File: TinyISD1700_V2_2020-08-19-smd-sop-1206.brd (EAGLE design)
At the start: 45.5 x 45.1 mm, 18 parts, among them IC3 LM317MDT, U1 ATTINY4313-SU

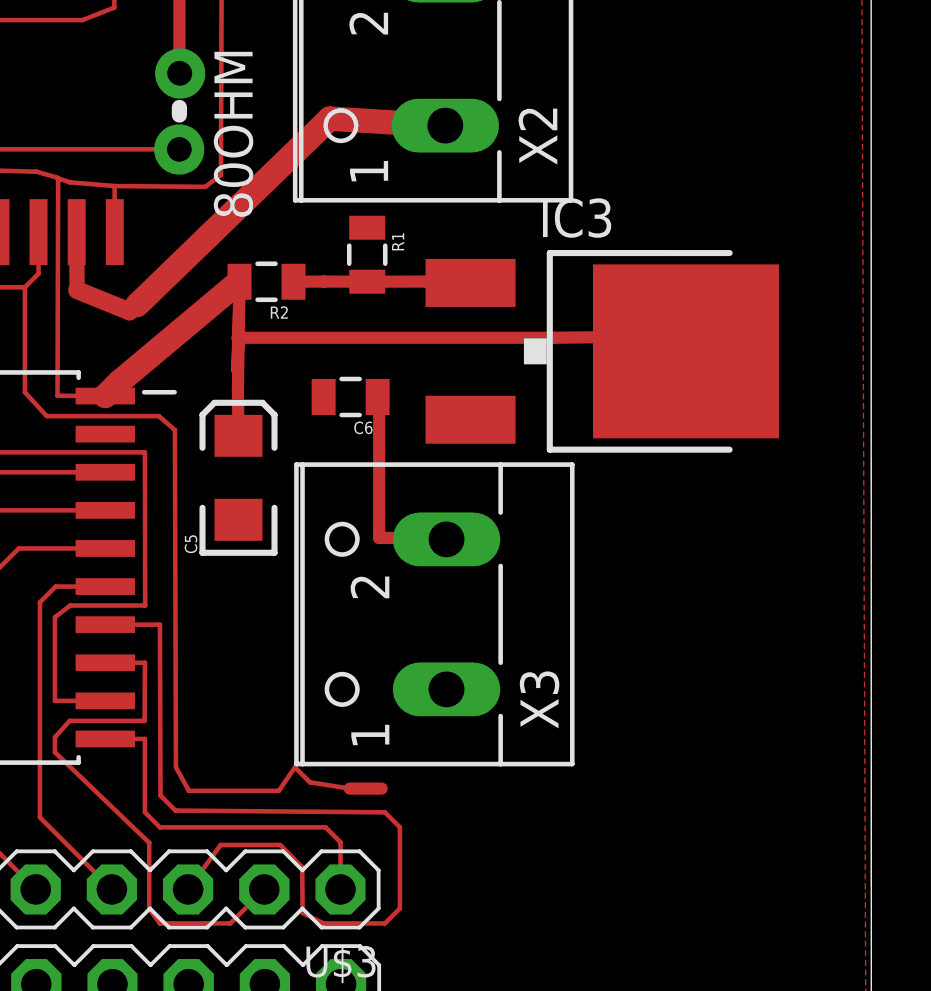
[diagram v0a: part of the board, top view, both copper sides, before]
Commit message: Resistors changed to 1205 factor
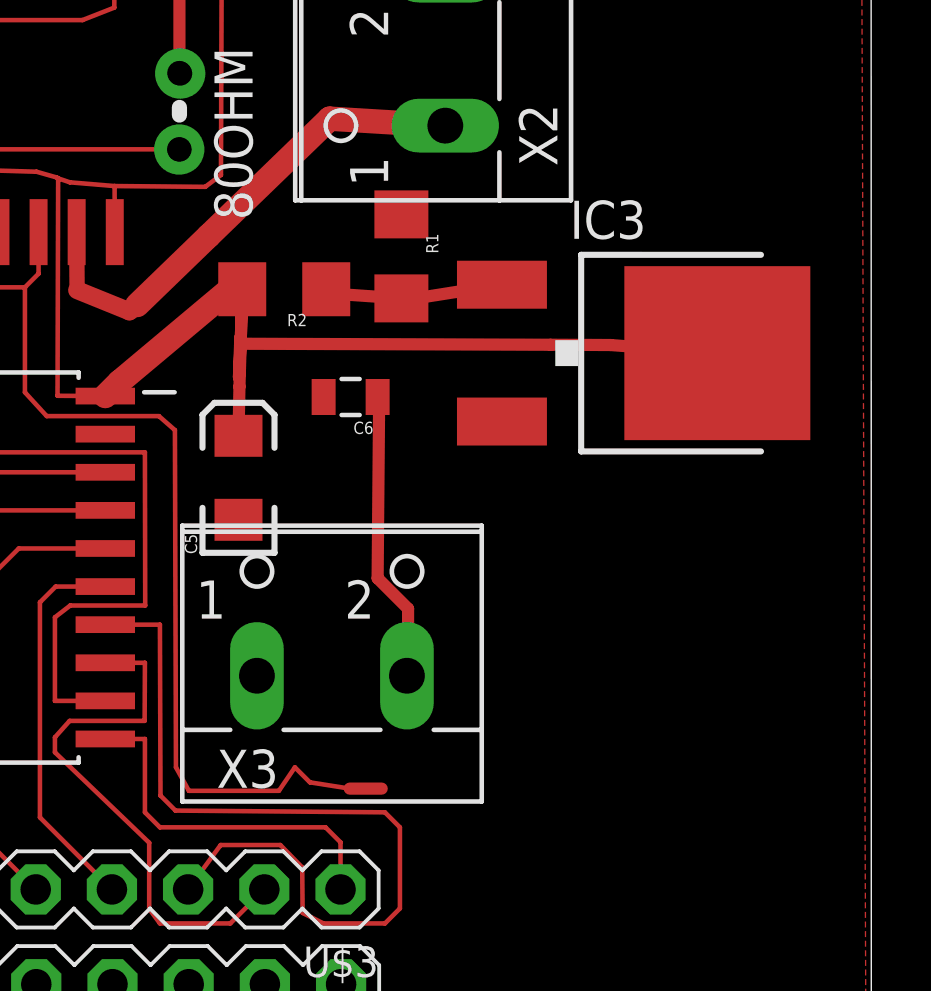
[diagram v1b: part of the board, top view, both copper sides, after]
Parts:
- R1, R2: device SparkFun2:0805 -> SparkFun:1206
- moved X3 2.67 mm to (25.5, 12.7), turned to 0 degrees
- moved R1 1.14 mm to (27.8, 25.5)
- moved IC3 1.05 mm to (36.0, 22.2)
- moved R2 0.64 mm to (23.9, 24.4)
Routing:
- net N$28: track 7.04 -> 9.80 mm
- net VCC: track 88.8 -> 89.8 mm
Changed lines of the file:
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@@
 <layer number="17" name="Pads" color="2" fill="1" visible="yes" active="yes"/>
 <layer number="18" name="Vias" color="2" fill="1" visible="yes" active="yes"/>
-<layer number="19" name="Unrouted" color="6" fill="1" visible="no" active="yes"/>
+<layer number="19" name="Unrouted" color="6" fill="1" visible="yes" active="yes"/>
 <layer number="20" name="Dimension" color="15" fill="1" visible="no" active="yes"/>
 <layer number="21" name="tPlace" color="7" fill="1" visible="no" active="yes"/>
 <layer number="22" name="bPlace" color="7" fill="1" visible="no" active="yes"/>
-<layer number="23" name="tOrigins" color="15" fill="1" visible="no" active="yes"/>
-<layer number="24" name="bOrigins" color="15" fill="1" visible="no" active="yes"/>
+<layer number="23" name="tOrigins" color="15" fill="1" visible="yes" active="yes"/>
+<layer number="24" name="bOrigins" color="15" fill="1" visible="yes" active="yes"/>
 <layer number="25" name="tNames" color="7" fill="1" visible="no" active="yes"/>
 <layer number="26" name="bNames" color="7" fill="1" visible="no" active="yes"/>
@@
 <attribute name="VALUE" x="35.6541875" y="27.271328125" size="1.27" layer="27" ratio="10" rot="R90"/>
 </element>
-<element name="X3" library="con-wago-500" package="W237-102" value="" x="28.07615" y="13.518975" smashed="yes" rot="R90">
-<attribute name="MF" value="" x="28.07615" y="13.518975" size="1.778" layer="27" rot="R90" display="off"/>
-<attribute name="MPN" value="" x="28.07615" y="13.518975" size="1.778" layer="27" rot="R90" display="off"/>
-<attribute name="NAME" x="33.07995" y="9.672775" size="1.27" layer="25" ratio="10" rot="R90"/>
-<attribute name="OC_FARNELL" value="unknown" x="28.07615" y="13.518975" size="1.778" layer="27" rot="R90" display="off"/>
-<attribute name="OC_NEWARK" value="70K9898" x="28.07615" y="13.518975" size="1.778" layer="27" rot="R90" display="off"/>
-<attribute name="VALUE" x="35.69615" y="8.478975" size="1.27" layer="27" ratio="10" rot="R90"/>
+<element name="X3" library="con-wago-500" package="W237-102" value="" x="25.525759375" y="12.74339375" smashed="yes">
+<attribute name="MF" value="" x="25.525759375" y="12.74339375" size="1.778" layer="27" display="off"/>
+<attribute name="MPN" value="" x="25.525759375" y="12.74339375" size="1.778" layer="27" display="off"/>
+<attribute name="NAME" x="21.679559375" y="7.73959375" size="1.27" layer="25" ratio="10"/>
+<attribute name="OC_FARNELL" value="unknown" x="25.525759375" y="12.74339375" size="1.778" layer="27" display="off"/>
+<attribute name="OC_NEWARK" value="70K9898" x="25.525759375" y="12.74339375" size="1.778" layer="27" display="off"/>
+<attribute name="VALUE" x="20.485759375" y="5.12339375" size="1.27" layer="27" ratio="10"/>
 </element>
 <element name="C6" library="SparkFun2" package="0805" value="" x="26.1483375" y="20.76579375" smashed="yes" rot="R180">
@@
 <attribute name="VALUE" x="27.1643375" y="22.16279375" size="0.4064" layer="27" rot="R180"/>
 </element>
-<element name="R1" library="SparkFun2" package="0805" value="" x="26.7023125" y="25.50895" smashed="yes" rot="R270">
-<attribute name="NAME" x="27.5278125" y="26.27095" size="0.4064" layer="25" rot="R270"/>
-<attribute name="VALUE" x="25.3053125" y="26.52495" size="0.4064" layer="27" rot="R270"/>
-</element>
-<element name="R2" library="SparkFun2" package="0805" value="" x="23.34449375" y="24.606784375" smashed="yes" rot="R180">
-<attribute name="NAME" x="24.10649375" y="23.781284375" size="0.4064" layer="25" rot="R180"/>
-<attribute name="VALUE" x="24.36049375" y="26.003784375" size="0.4064" layer="27" rot="R180"/>
+<element name="R1" library="SparkFun" package="1206" value="" x="27.840146875" y="25.45298125" smashed="yes" rot="R270">
+<attribute name="NAME" x="28.665646875" y="26.21498125" size="0.4064" layer="25" rot="R270"/>
+<attribute name="VALUE" x="26.443146875" y="26.46898125" size="0.4064" layer="27" rot="R270"/>
+</element>
+<element name="R2" library="SparkFun" package="1206" value="" x="23.93505625" y="24.358078125" smashed="yes" rot="R180">
+<attribute name="NAME" x="24.69705625" y="23.532578125" size="0.4064" layer="25" rot="R180"/>
+<attribute name="VALUE" x="24.95105625" y="25.755078125" size="0.4064" layer="27" rot="R180"/>
 </element>
 <element name="C5" library="SparkFun2" package="EIA3216" value="" x="22.410459375" y="18.071790625" smashed="yes" rot="R90">
@@
 <attribute name="VALUE" x="21.078459375" y="18.479790625" size="0.4064" layer="27" rot="R90"/>
 </element>
-<element name="IC3" library="v-reg" package="DPACK" value="LM317MDT" x="34.94599375" y="22.287078125" rot="R270"/>
+<element name="IC3" library="v-reg" package="DPACK" value="LM317MDT" x="35.991984375" y="22.228065625" rot="R270"/>
 <element name="U$1" library="arduino" package="8PIN_HEADER" value="8PIN_HEADER" x="8.050165625" y="1.192378125">
 <attribute name="MPN" value="YSDKS128E10" x="8.050165625" y="1.192378125" size="1.778" layer="27" display="off"/>
@@
 <contactref element="R2" pad="2"/>
 <contactref element="C5" pad="A"/>
-<wire x1="22.44449375" y1="24.606784375" x2="22.390965625" y2="20.996465625" width="0.4064" layer="1"/>
-<wire x1="22.410459375" y1="19.471790625" x2="22.390965625" y2="20.996465625" width="0.4064" layer="1"/>
-<wire x1="22.44449375" y1="24.606784375" x2="22.29029375" y2="24.49384375" width="0.4064" layer="1"/>
-<wire x1="22.44449375" y1="24.606784375" x2="22.400828125" y2="22.8057875" width="0.4064" layer="1"/>
-<wire x1="22.400828125" y1="22.8057875" x2="22.37325" y2="21.668340625" width="0.4064" layer="1"/>
-<wire x1="22.37325" y1="21.668340625" x2="22.4187875" y2="22.989696875" width="0.4064" layer="1"/>
+<wire x1="22.53505625" y1="24.358078125" x2="22.442771875" y2="21.113009375" width="0.4064" layer="1"/>
+<wire x1="22.410459375" y1="19.471790625" x2="22.442771875" y2="21.113009375" width="0.4064" layer="1"/>
+<wire x1="22.53505625" y1="24.358078125" x2="22.29029375" y2="24.49384375" width="0.4064" layer="1"/>
+<wire x1="22.53505625" y1="24.358078125" x2="22.491484375" y2="22.7928375" width="0.4064" layer="1"/>
+<wire x1="22.491484375" y1="22.7928375" x2="22.425053125" y2="21.422303125" width="0.4064" layer="1"/>
+<wire x1="22.425053125" y1="21.422303125" x2="22.470590625" y2="22.743659375" width="0.4064" layer="1"/>
 <contactref element="IC3" pad="4"/>
-<wire x1="37.32599375" y1="22.287078125" x2="34.856428125" y2="22.7624625" width="0.4064" layer="1"/>
-<wire x1="34.856428125" y1="22.7624625" x2="32.916465625" y2="22.740228125" width="0.4064" layer="1"/>
-<wire x1="32.916465625" y1="22.740228125" x2="22.381428125" y2="22.740228125" width="0.4064" layer="1"/>
-<wire x1="22.381428125" y1="22.740228125" x2="22.400828125" y2="22.8057875" width="0.4064" layer="1"/>
+<wire x1="38.371984375" y1="22.228065625" x2="34.814984375" y2="22.4982875" width="0.4064" layer="1"/>
+<wire x1="34.814984375" y1="22.4982875" x2="32.81285625" y2="22.507140625" width="0.4064" layer="1"/>
+<wire x1="32.81285625" y1="22.507140625" x2="22.472084375" y2="22.540746875" width="0.4064" layer="1"/>
+<wire x1="22.472084375" y1="22.540746875" x2="22.491484375" y2="22.7928375" width="0.4064" layer="1"/>
 </signal>
 <signal name="Q">
@@
 <contactref element="R1" pad="2"/>
 <contactref element="R2" pad="1"/>
-<wire x1="24.24449375" y1="24.606784375" x2="25.2648625" y2="24.61429375" width="0.4064" layer="1"/>
-<wire x1="25.2648625" y1="24.61429375" x2="26.7023125" y2="24.60895" width="0.4064" layer="1"/>
-<wire x1="26.7023125" y1="24.60895" x2="28.741184375" y2="24.61429375" width="0.4064" layer="1"/>
+<wire x1="25.33505625" y1="24.358078125" x2="25.135353125" y2="24.238765625" width="0.4064" layer="1"/>
+<wire x1="25.135353125" y1="24.238765625" x2="27.840146875" y2="24.05298125" width="0.4064" layer="1"/>
+<wire x1="27.840146875" y1="24.05298125" x2="27.938225" y2="23.91503125" width="0.4064" layer="1"/>
 <contactref element="IC3" pad="1"/>
-<wire x1="30.14599375" y1="24.567078125" x2="28.741184375" y2="24.567078125" width="0.4064" layer="1"/>
-<wire x1="28.741184375" y1="24.567078125" x2="28.741184375" y2="24.61429375" width="0.4064" layer="1"/>
+<wire x1="31.191984375" y1="24.508065625" x2="28.041834375" y2="24.010259375" width="0.4064" layer="1"/>
+<wire x1="28.041834375" y1="24.010259375" x2="27.938225" y2="23.91503125" width="0.4064" layer="1"/>
 </signal>
 <signal name="N$28">
@@
 <contactref element="X3" pad="2"/>
 <wire x1="27.0483375" y1="20.76579375" x2="27.099721875" y2="20.76579375" width="0.4064" layer="1"/>
-<wire x1="27.099721875" y1="20.76579375" x2="27.099721875" y2="16.069553125" width="0.4064" layer="1"/>
-<wire x1="27.099721875" y1="16.069553125" x2="29.34615" y2="16.069553125" width="0.4064" layer="1"/>
-<wire x1="29.34615" y1="16.069553125" x2="29.34615" y2="16.018975" width="0.4064" layer="1"/>
+<wire x1="27.04791875" y1="14.723665625" x2="27.099721875" y2="20.76579375" width="0.4064" layer="1"/>
+<wire x1="28.025759375" y1="11.47339375" x2="28.06376875" y2="11.47339375" width="0.4064" layer="1"/>
+<wire x1="28.06376875" y1="11.47339375" x2="28.06376875" y2="13.707815625" width="0.4064" layer="1"/>
+<wire x1="28.06376875" y1="13.707815625" x2="27.04791875" y2="14.723665625" width="0.4064" layer="1"/>
 </signal>
 </signals>
